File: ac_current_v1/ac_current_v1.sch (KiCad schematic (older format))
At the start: 32 parts, among them J1 ICSP, J2 UART, J3 AC1_IN, J4 AC1_OUT, J5 AC2_IN, J6 AC2_OUT, J7 GMS1005, J8 AC_SLCT_2, J9 AC_SLCT_1, U1 NRF24L01_Breakout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

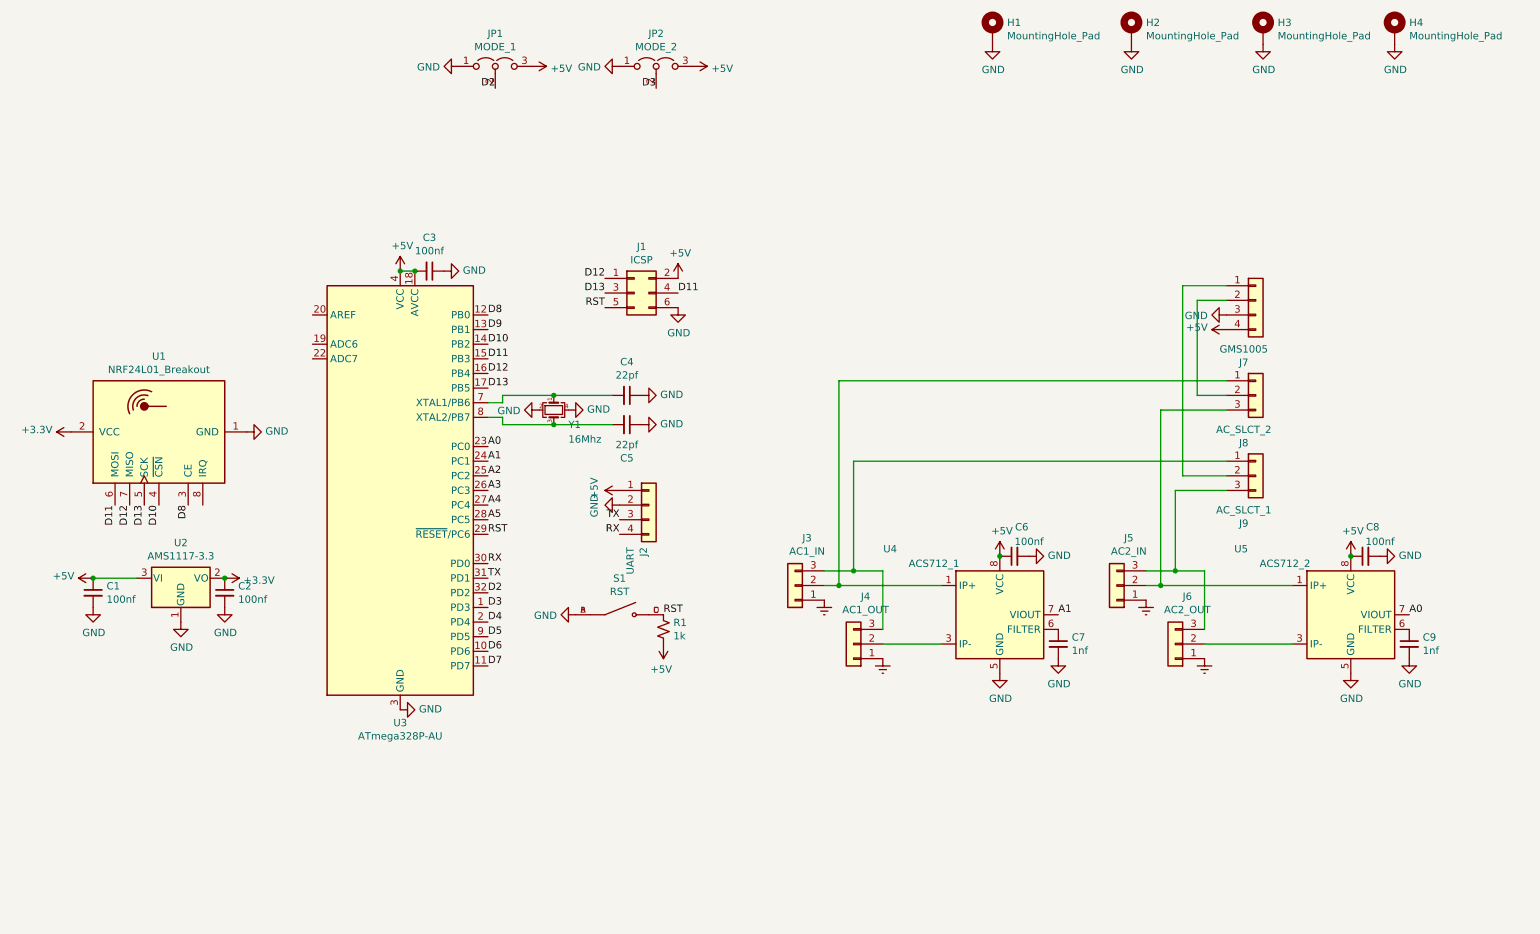
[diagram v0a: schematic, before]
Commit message: PCB Update(Added Sensor)
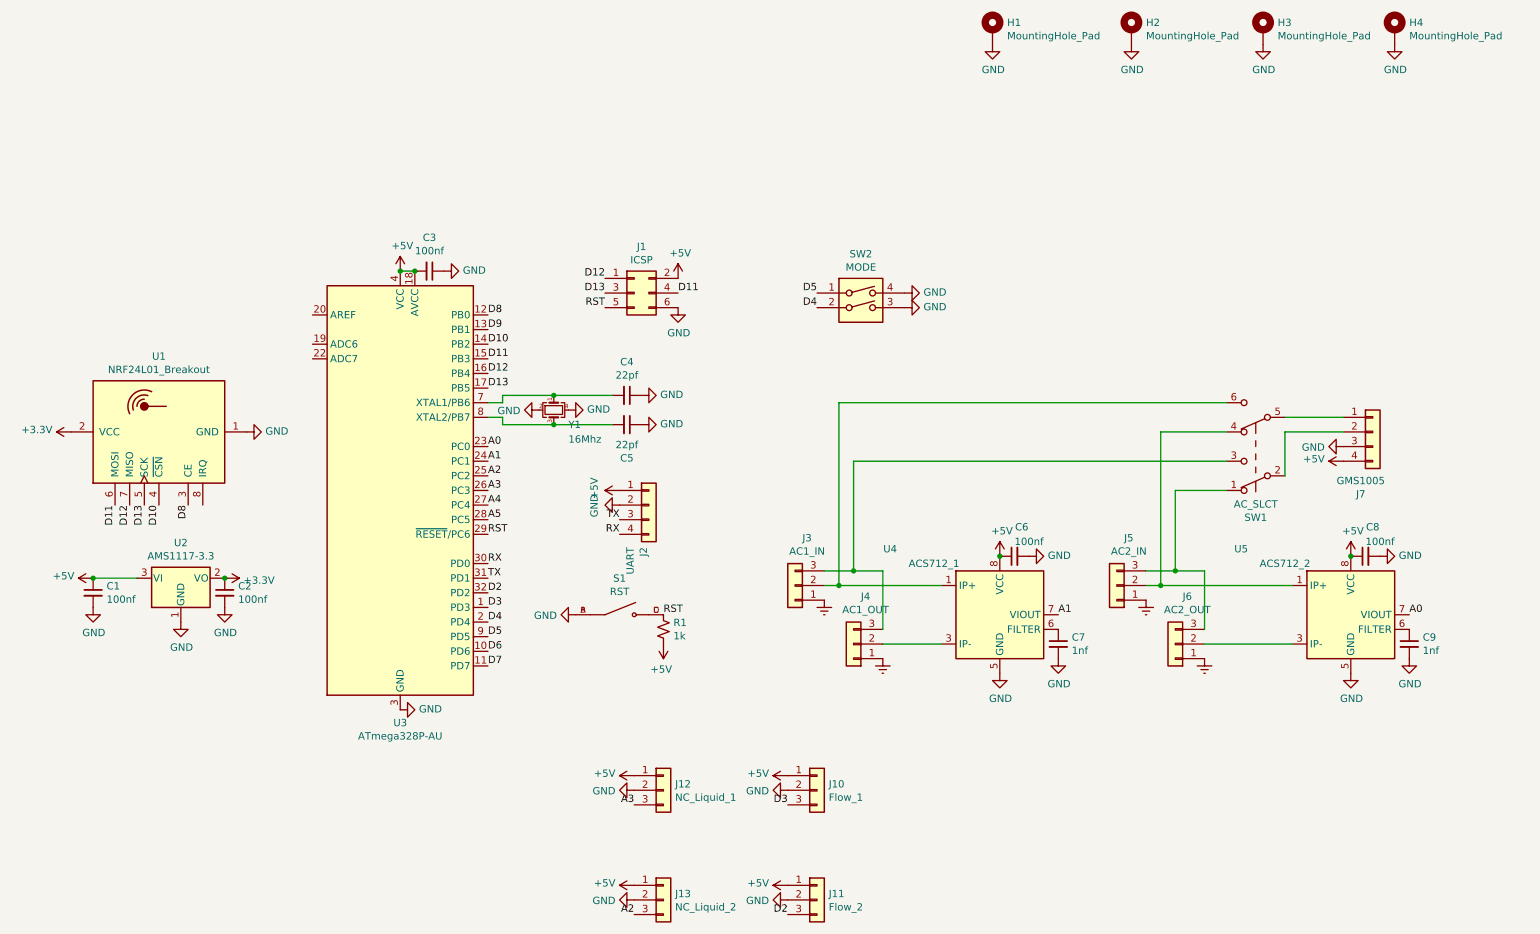
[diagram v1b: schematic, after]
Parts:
- removed J8: AC_SLCT_2, Connector_PinHeader_2.54mm:PinHeader_1x03_P2.54mm_Vertical, symbol Connector_Generic:Conn_01x03
- removed J9: AC_SLCT_1, Connector_PinHeader_2.54mm:PinHeader_1x03_P2.54mm_Vertical, symbol Connector_Generic:Conn_01x03
- removed JP1: MODE_1, Connector_PinHeader_2.54mm:PinHeader_1x03_P2.54mm_Vertical, symbol Jumper:Jumper_3_Open
- removed JP2: MODE_2, Connector_PinHeader_2.54mm:PinHeader_1x03_P2.54mm_Vertical, symbol Jumper:Jumper_3_Open
- added J10: Flow_1, Connector_Molex:Molex_PicoBlade_53261-0371_1x03-1MP_P1.25mm_Horizontal, symbol Connector_Generic:Conn_01x03
- added J11: Flow_2, Connector_Molex:Molex_PicoBlade_53261-0371_1x03-1MP_P1.25mm_Horizontal, symbol Connector_Generic:Conn_01x03
- added J12: NC_Liquid_1, Connector_Molex:Molex_PicoBlade_53261-0371_1x03-1MP_P1.25mm_Horizontal, symbol Connector_Generic:Conn_01x03
- added J13: NC_Liquid_2, Connector_Molex:Molex_PicoBlade_53261-0371_1x03-1MP_P1.25mm_Horizontal, symbol Connector_Generic:Conn_01x03
- added SW1: AC_SLCT, KIcad:MTS-202, symbol Switch:SW_Push_DPDT
- added SW2: MODE, KIcad:DSHP02TSGER, symbol Switch:SW_DIP_x02
- J3, J4, J5, J6: footprint KIcad:BR-762C_3 -> KIcad:SMD_762
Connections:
- net +5V: now also J10.1 (Pin_1), J11.1 (Pin_1), J12.1 (Pin_1), J13.1 (Pin_1)
- net A2: now also J13.3 (Pin_3)
- net A3: now also J12.3 (Pin_3)
- net D2: now also J11.3 (Pin_3)
- net D3: now also J10.3 (Pin_3)
- net D4: now also SW2.2
- net D5: now also SW2.1
- net GND: now also J10.2 (Pin_2), J11.2 (Pin_2), J12.2 (Pin_2), J13.2 (Pin_2), SW2.3, SW2.4
- net at J3.2 (Pin_2), U4.1 (IP+), U4.2 (IP+): now also SW1.6 (C)
- net at J3.3 (Pin_3), J4.3 (Pin_3): now also SW1.3 (C)
- net at J5.2 (Pin_2), U5.1 (IP+), U5.2 (IP+): now also SW1.4 (A)
- net at J5.3 (Pin_3), J6.3 (Pin_3): now also SW1.1 (A)
- net at J7.1 (Pin_1): now also SW1.5 (B)
- net at J7.2 (Pin_2): now also SW1.2 (B)
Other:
- moved on the sheet: J7
